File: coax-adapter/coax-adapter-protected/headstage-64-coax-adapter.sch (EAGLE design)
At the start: 10 parts, among them J1 X.FL-R-SMT-1(02), U1 TPS82085

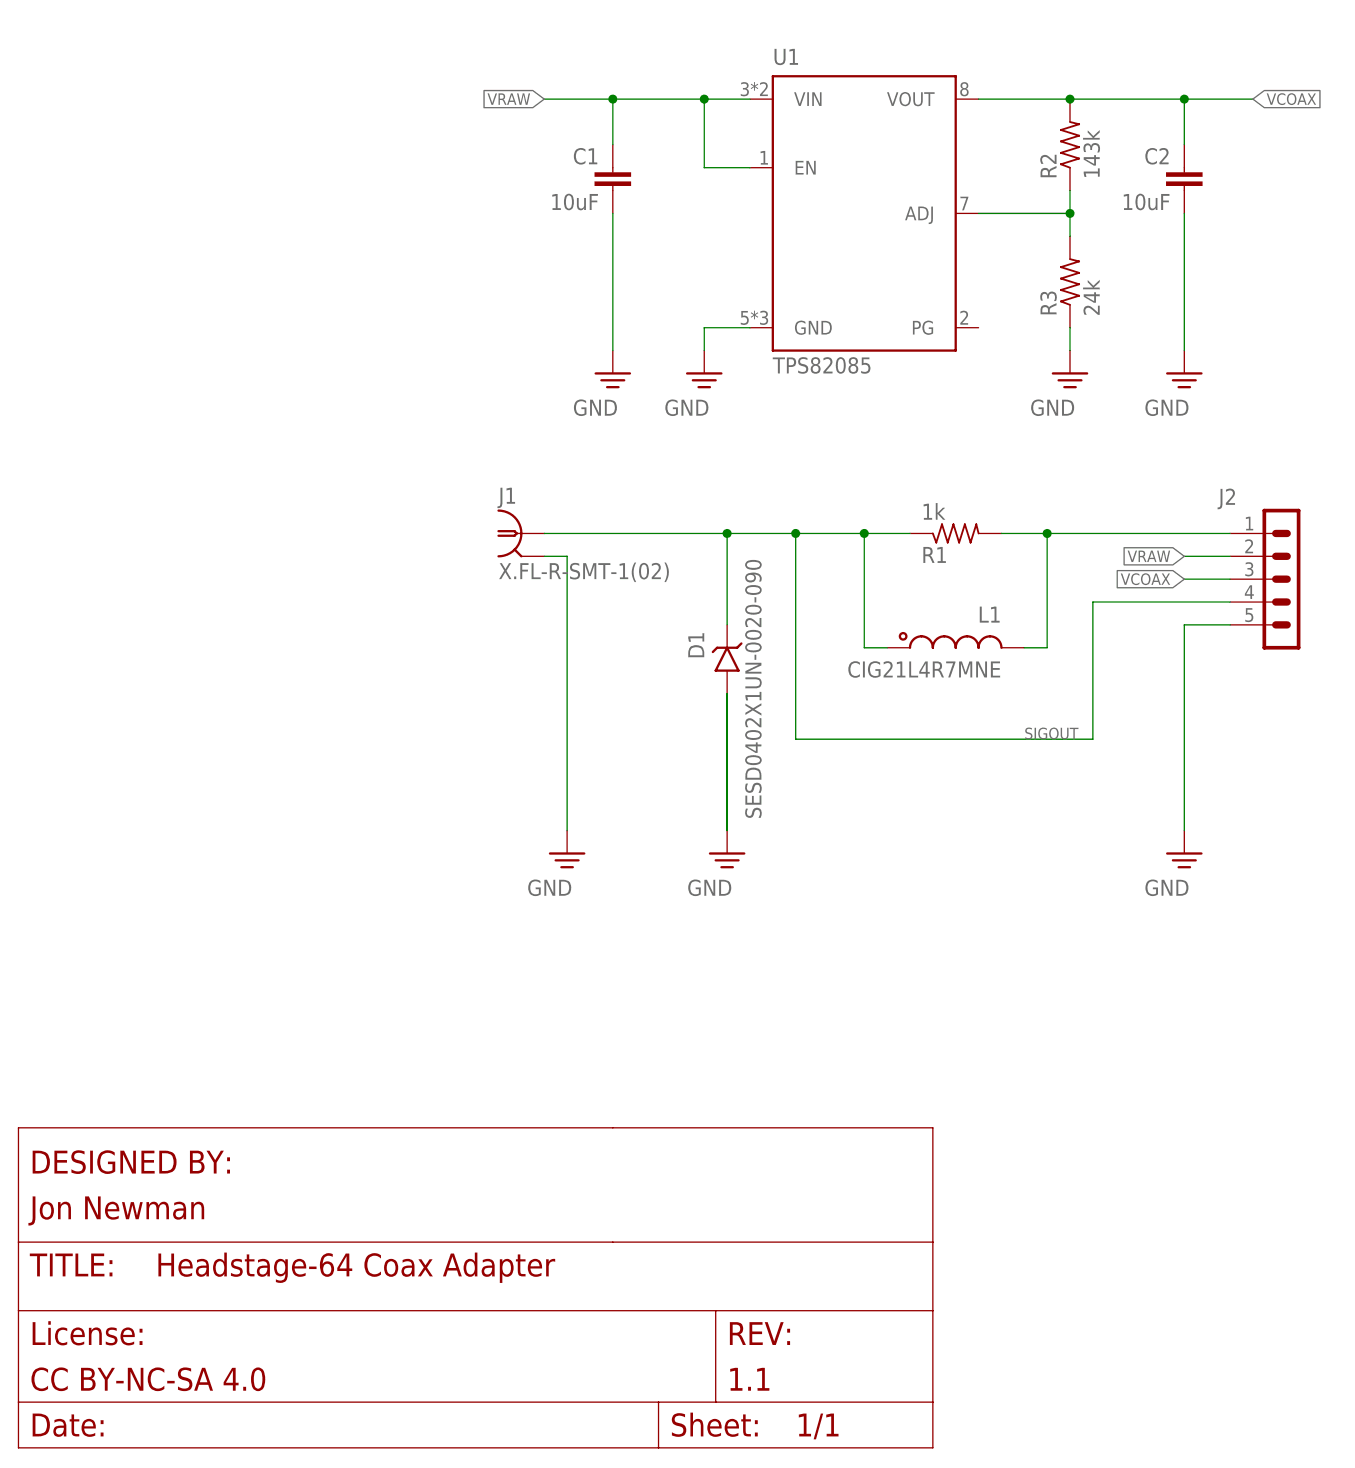
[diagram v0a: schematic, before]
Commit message: Over-voltage protection version of coax-adapter
- Also, general repo clean up, README edits, etc
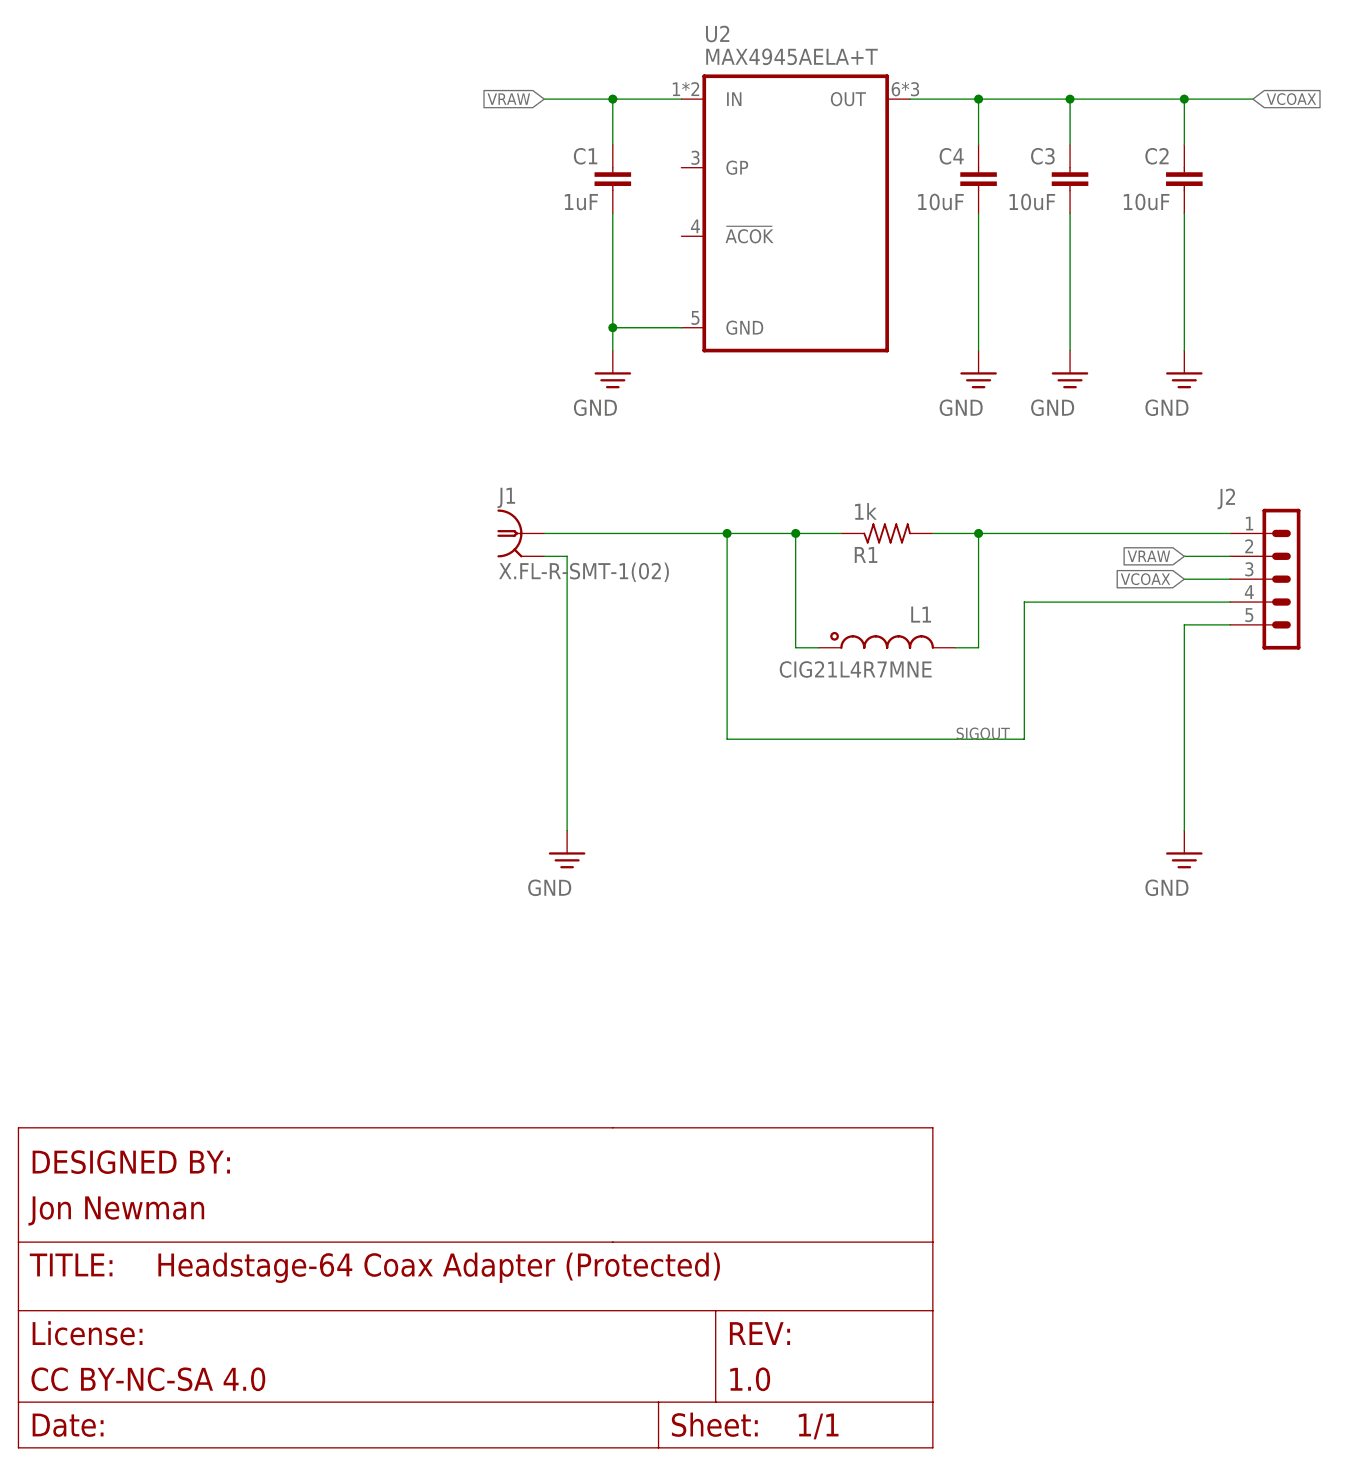
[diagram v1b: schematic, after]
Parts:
- removed D1: SESD0402X1UN-0020-090, jonnew:Z-DIODE_0402T-DFN
- removed R2: 143k, jonnew:R_0201T
- removed R3: 24k, jonnew:R_0201T
- removed U1: TPS82085, jonnew:TPS8208X
- added C3, C4: 10uF, jonnew:C_0603T
- added U2: MAX4945AELA+T, jonnew:MAX494X
- C1: value 10uF -> 1uF
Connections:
- removed net N$2: R2.1, R3.2, U1.ADJ
- net GND: now also C3.2, C4.2, U2.GND; no longer D1.A, R3.1, U1.GND
- net SIGOUT: no longer D1.C
- net VCOAX: now also C3.1, C4.1, U2.OUT; no longer R2.2, U1.VOUT
- net VRAW: now also U2.IN; no longer U1.EN, U1.VIN
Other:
- moved on the sheet: L1, R1

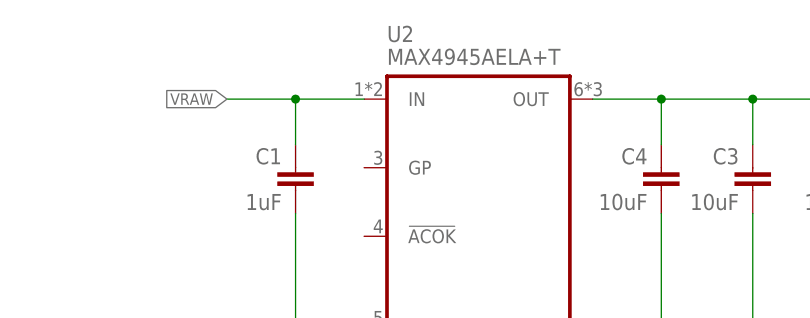
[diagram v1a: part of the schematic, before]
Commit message: Correct part numbers in protected coax-adapter.
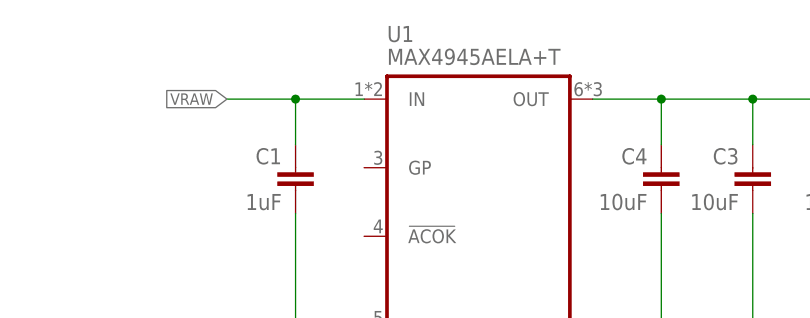
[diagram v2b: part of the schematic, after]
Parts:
- renumbered U2 to U1
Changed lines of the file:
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@@
 <part name="SUPPLY6" library="jonnew" deviceset="GND" device=""/>
 <part name="J2" library="jonnew" deviceset="PINHD-1X5" device="_HEADSTAGE-64-REV1.4-DAUGHTER-CARD-CASTELLATED"/>
-<part name="U2" library="jonnew" deviceset="MAX494X" device="" value="MAX4945AELA+T"/>
+<part name="U1" library="jonnew" deviceset="MAX494X" device="" value="MAX4945AELA+T"/>
 <part name="C3" library="jonnew" deviceset="C" device="_0603T" value="10uF">
 <attribute name="PARTNO" value="CL05A475MO5NUNC"/>
@@
 <instance part="SUPPLY6" gate="PE" x="134.62" y="124.46"/>
 <instance part="J2" gate="G$1" x="142.24" y="101.6"/>
-<instance part="U2" gate="G$1" x="91.44" y="142.24"/>
+<instance part="U1" gate="G$1" x="91.44" y="142.24"/>
 <instance part="C3" gate="C" x="121.92" y="147.32" smashed="yes" rot="MR0">
 <attribute name="PARTNO" x="121.92" y="147.32" size="1.27" layer="96" rot="MR0" display="off"/>
@@
 <wire x1="71.12" y1="142.24" x2="71.12" y2="129.54" width="0.1524" layer="91"/>
 <pinref part="SUPPLY2" gate="PE" pin="GND"/>
-<pinref part="U2" gate="G$1" pin="GND"/>
+<pinref part="U1" gate="G$1" pin="GND"/>
 <wire x1="71.12" y1="129.54" x2="71.12" y2="127" width="0.1524" layer="91"/>
 <wire x1="78.74" y1="129.54" x2="71.12" y2="129.54" width="0.1524" layer="91"/>
@@
 <wire x1="71.12" y1="149.86" x2="71.12" y2="154.94" width="0.1524" layer="91"/>
 <label x="63.5" y="154.94" size="1.27" layer="95" rot="R180" xref="yes"/>
-<pinref part="U2" gate="G$1" pin="IN"/>
+<pinref part="U1" gate="G$1" pin="IN"/>
 <wire x1="71.12" y1="154.94" x2="78.74" y2="154.94" width="0.1524" layer="91"/>
 <junction x="71.12" y="154.94"/>
@@
 <junction x="134.62" y="154.94"/>
 <label x="142.24" y="154.94" size="1.27" layer="95" xref="yes"/>
-<pinref part="U2" gate="G$1" pin="OUT"/>
+<pinref part="U1" gate="G$1" pin="OUT"/>
 <pinref part="C4" gate="C" pin="1"/>
 <wire x1="111.76" y1="154.94" x2="111.76" y2="149.86" width="0.1524" layer="91"/>
